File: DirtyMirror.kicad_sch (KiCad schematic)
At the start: 72 parts, among them J101 PWR, J102 ScopeGroundLoop, SW101 SW_SPDT, U101 TL074, U102 TL074

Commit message: threshold/summing amp value tweaks
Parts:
- R101, R107: value 56k -> 47k
- R103, R106: value 68k -> 51k
- R112: value 51k -> 5k1
- R113, R116: value 56k -> 5k6
- R118, R120: value 51k -> 47k
- R119, R121: value 68k -> 56k
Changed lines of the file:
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@@
 			)
 		)
-		(property "Value" "56k"
+		(property "Value" "5k6"
 			(at 211.582 69.85 90)
 			(effects
@@
 			)
 		)
-		(property "Value" "56k"
+		(property "Value" "5k6"
 			(at 211.582 53.34 90)
 			(effects
@@
 			)
 		)
-		(property "Value" "68k"
+		(property "Value" "56k"
 			(at 210.058 92.71 90)
 			(effects
@@
 			)
 		)
-		(property "Value" "51k"
+		(property "Value" "5k1"
 			(at 211.582 62.23 90)
 			(effects
@@
 			)
 		)
-		(property "Value" "51k"
+		(property "Value" "47k"
 			(at 210.058 101.6 90)
 			(effects
@@
 			)
 		)
-		(property "Value" "68k"
+		(property "Value" "51k"
 			(at 52.07 236.9819 0)
 			(effects
@@
 			)
 		)
-		(property "Value" "56k"
+		(property "Value" "47k"
 			(at 76.2 236.9819 0)
 			(effects
@@
 			)
 		)
-		(property "Value" "68k"
+		(property "Value" "51k"
 			(at 76.2 218.9479 0)
 			(effects
@@
 			)
 		)
-		(property "Value" "51k"
+		(property "Value" "47k"
 			(at 210.058 83.82 90)
 			(effects
@@
 			)
 		)
-		(property "Value" "68k"
+		(property "Value" "56k"
 			(at 228.6 83.82 90)
 			(effects
@@
 			)
 		)
-		(property "Value" "56k"
+		(property "Value" "47k"
 			(at 52.07 219.2019 0)
 			(effects

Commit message: optimized rev2 component values :)
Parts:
- R112: value 5k1 -> 51k
- R113, R116: value 5k6 -> 56k
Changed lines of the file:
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@@
 			)
 		)
-		(property "Value" "5k6"
+		(property "Value" "56k"
 			(at 211.582 69.85 90)
 			(effects
@@
 			)
 		)
-		(property "Value" "5k6"
+		(property "Value" "56k"
 			(at 211.582 53.34 90)
 			(effects
@@
 			)
 		)
-		(property "Value" "5k1"
+		(property "Value" "51k"
 			(at 211.582 62.23 90)
 			(effects

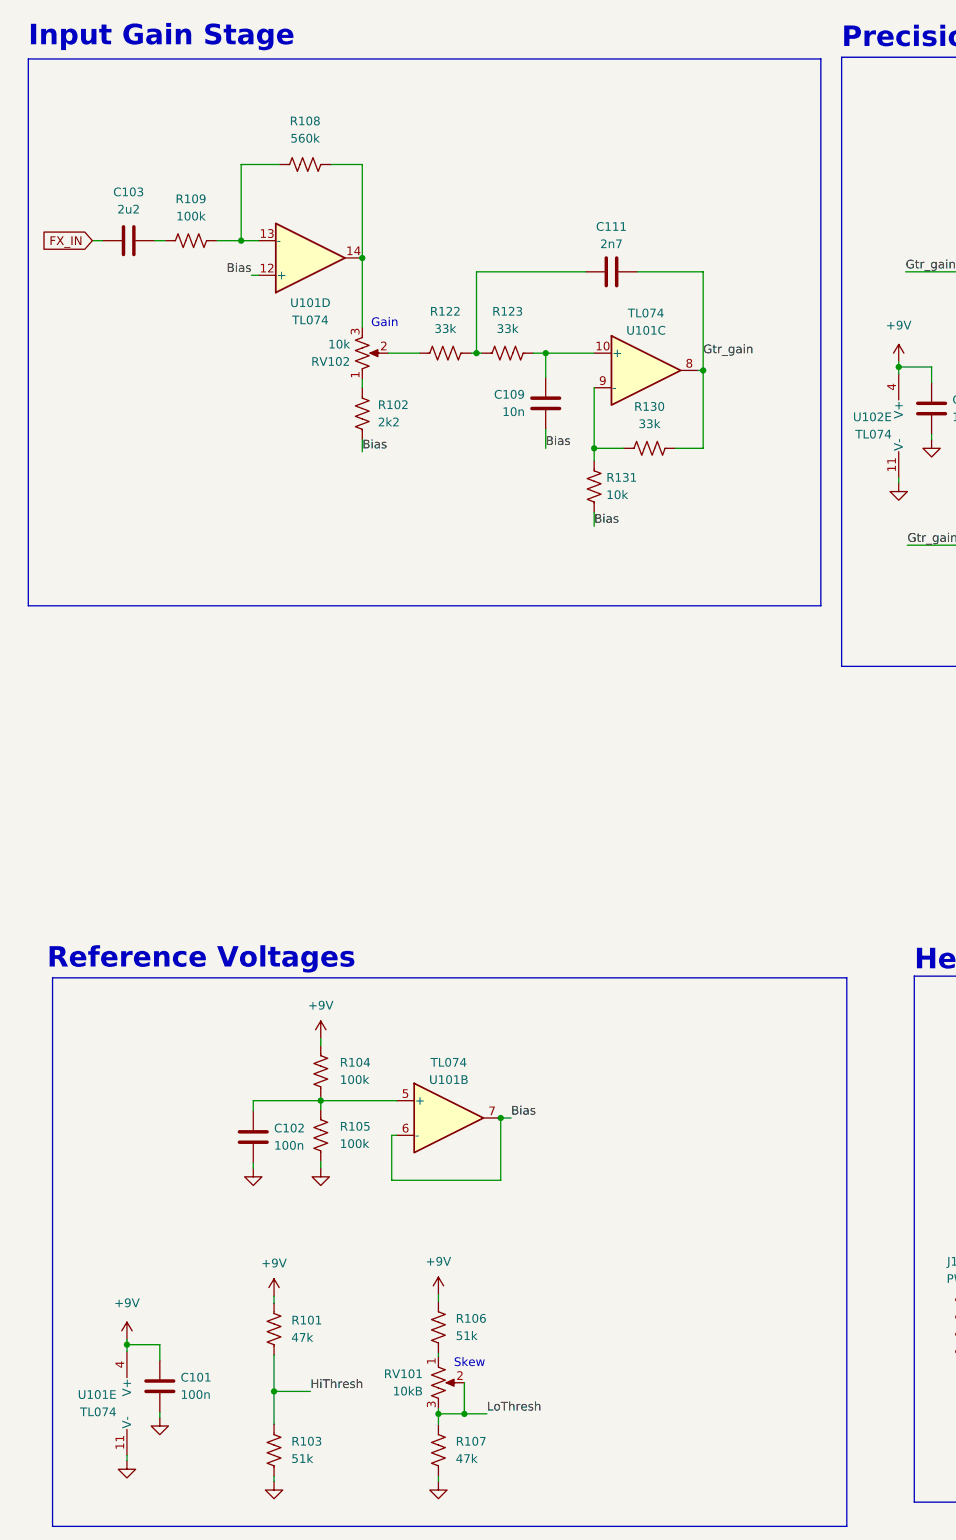
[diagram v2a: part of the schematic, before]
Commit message: moved skew control to input amp
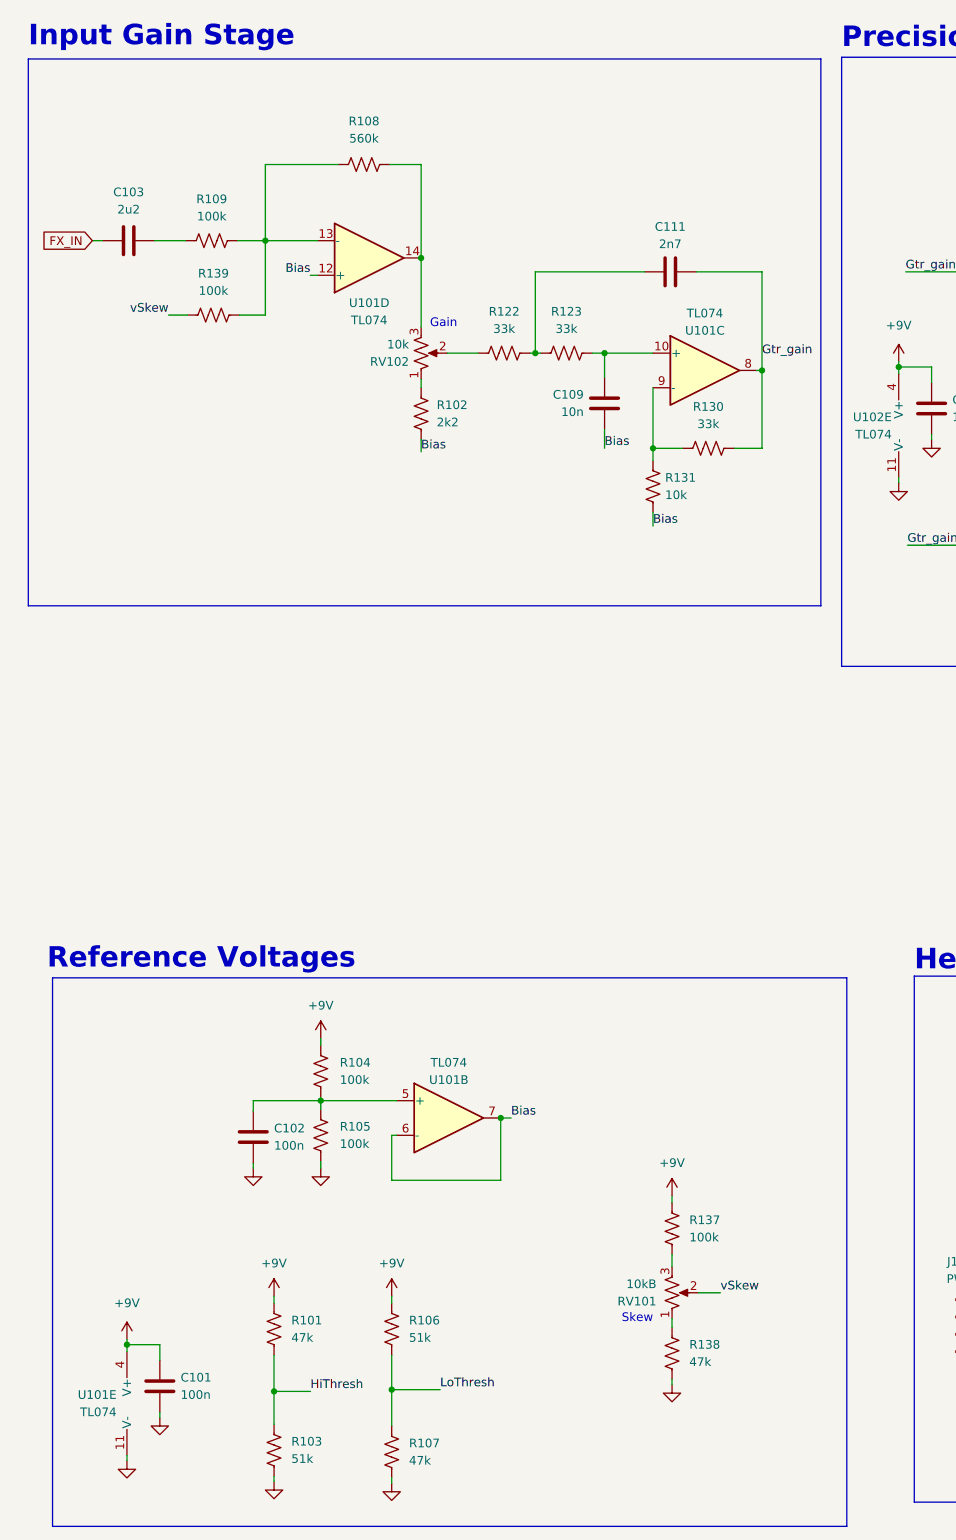
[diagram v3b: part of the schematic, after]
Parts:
- added R137, R139: 100k, Resistor_SMD:R_0805_2012Metric, symbol Device:R_US
- added R138: 47k, Resistor_SMD:R_0805_2012Metric, symbol Device:R_US
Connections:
- net +9V: now also R137.1
- net GND: now also R138.2
- net LoThresh: now also R106.2; no longer RV101.2, RV101.3
- net at R108.1, R109.2, U101.13 (-): now also R139.2
- net at RV101.1: now also R138.1; no longer R106.2
- new net: R137.2, RV101.3
- new net vSkew: R139.1, RV101.2
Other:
- moved on the sheet: C109, C111, R102, R106, R107, R108, R109, R122, R123, R130, R131, RV101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

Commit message: rev3 minor tweaks
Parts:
- added TP112: SKEW, TestPoint:TestPoint_THTPad_D2.0mm_Drill1.0mm_VAL, symbol Connector:TestPoint
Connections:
- net vSkew: now also TP112.1
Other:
- note added: "Test Points"
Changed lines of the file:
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@@
 	(wire
 		(pts
+			(xy 241.554 194.056) (xy 242.57 194.056)
+		)
+		(stroke
+			(width 0)
+			(type default)
+		)
+	)
+	(wire
+		(pts
 			(xy 107.95 216.408) (xy 107.95 217.678)
 		)
@@
 	(wire
 		(pts
+			(xy 241.554 192.024) (xy 241.554 194.056)
+		)
+		(stroke
+			(width 0)
+			(type default)
+		)
+	)
+	(wire
+		(pts
 			(xy 206.502 56.642) (xy 207.772 56.642)
 		)
@@
 		)
 	)
+	(text "Test Points"
+		(exclude_from_sim no)
+		(at 188.468 163.83 0)
+		(effects
+			(font
+				(size 3 3)
+				(thickness 0.6)
+				(bold yes)
+			)
+			(justify left)
+		)
+	)
 	(text "Header  & LED"
 		(exclude_from_sim no)
@@
 		)
 	)
+	(label "vSkew"
+		(at 242.57 194.056 0)
+		(fields_autoplaced yes)
+		(effects
+			(font
+				(size 1.27 1.27)
+			)
+			(justify left bottom)
+		)
+	)
 	(label "LoRect"
 		(at 230.378 177.038 0)
@@
 					(unit 1)
 				)
+			)
+		)
+	)
+	(symbol
+		(lib_id "Connector:TestPoint")
+		(at 241.554 192.024 0)
+		(unit 1)
+		(exclude_from_sim no)
+		(in_bom no)
+		(on_board yes)
+		(dnp no)
+		(fields_autoplaced yes)
+		(property "Reference" "TP112"
+			(at 243.84 187.4519 0)
+			(effects
+				(font
+					(size 1.27 1.27)
+				)
+				(justify left)
+			)
+		)
+		(property "Value" "SKEW"
+			(at 243.84 189.9919 0)
+			(effects
+				(font
+					(size 1.27 1.27)
+				)
+				(justify left)
+			)
+		)
+		(property "Footprint" "TestPoint:TestPoint_THTPad_D2.0mm_Drill1.0mm_VAL"
+			(at 246.634 192.024 0)
+			(effects
+				(font
+					(size 1.27 1.27)
+				)
+				(hide yes)
+			)
+		)
+		(property "Datasheet" "~"
+			(at 246.634 192.024 0)
+			(effects
+				(font
+					(size 1.27 1.27)
+				)
+				(hide yes)
+			)
+		)
+		(property "Description" "test point"
+			(at 241.554 192.024 0)
+			(effects
+				(font
+					(size 1.27 1.27)
+				)
+				(hide yes)
+			)
+		)
+		(pin "1"
+		)
+		(instances
+			(project "DirtyMirror"
+				(path "/46809a99-6cea-45df-9493-947f7ec228cb"
+					(reference "TP112")
+					(unit 1)
+				)
